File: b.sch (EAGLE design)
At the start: 64 parts, among them CN1 CON-2P-DG500-5.08, CN2 CON-3P-DG500-5.08, CN3 CON-2P-DG500-5.08, CN4 CON-3P-DG500-5.08, CN5 CON-2P-DG500-5.08, Q1 BCR133, U2 TPS563200, U3 ISO3082, U4 B1212S-1WR3, U5 L78L05ACD13TR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

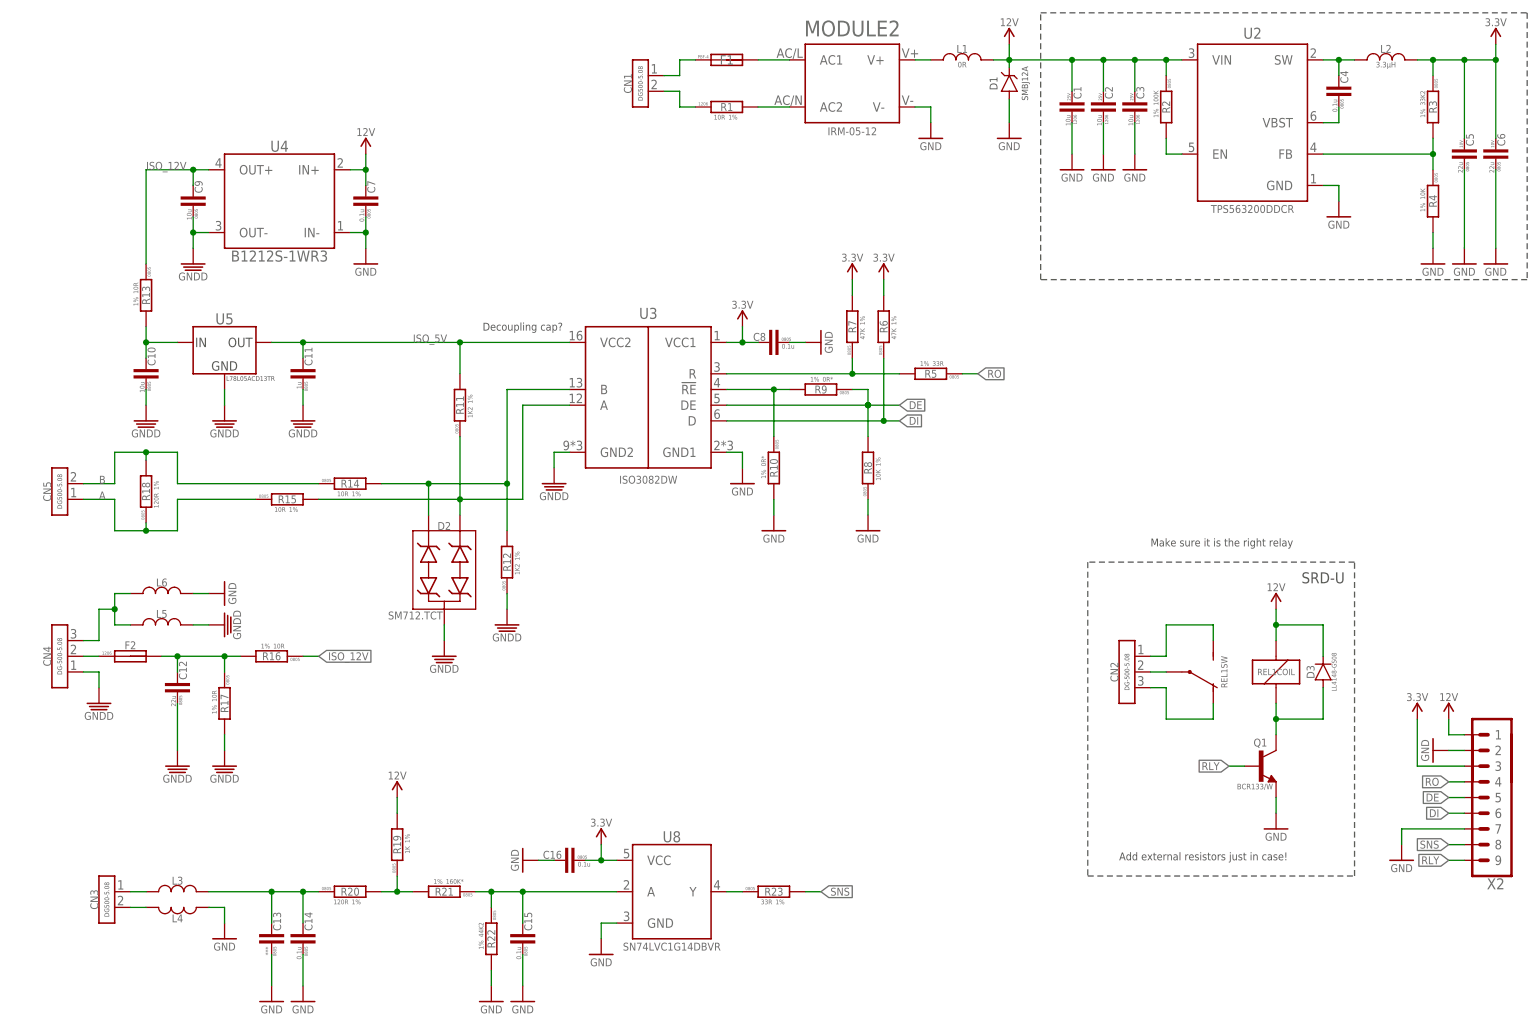
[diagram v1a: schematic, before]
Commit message: Notes and pictures update
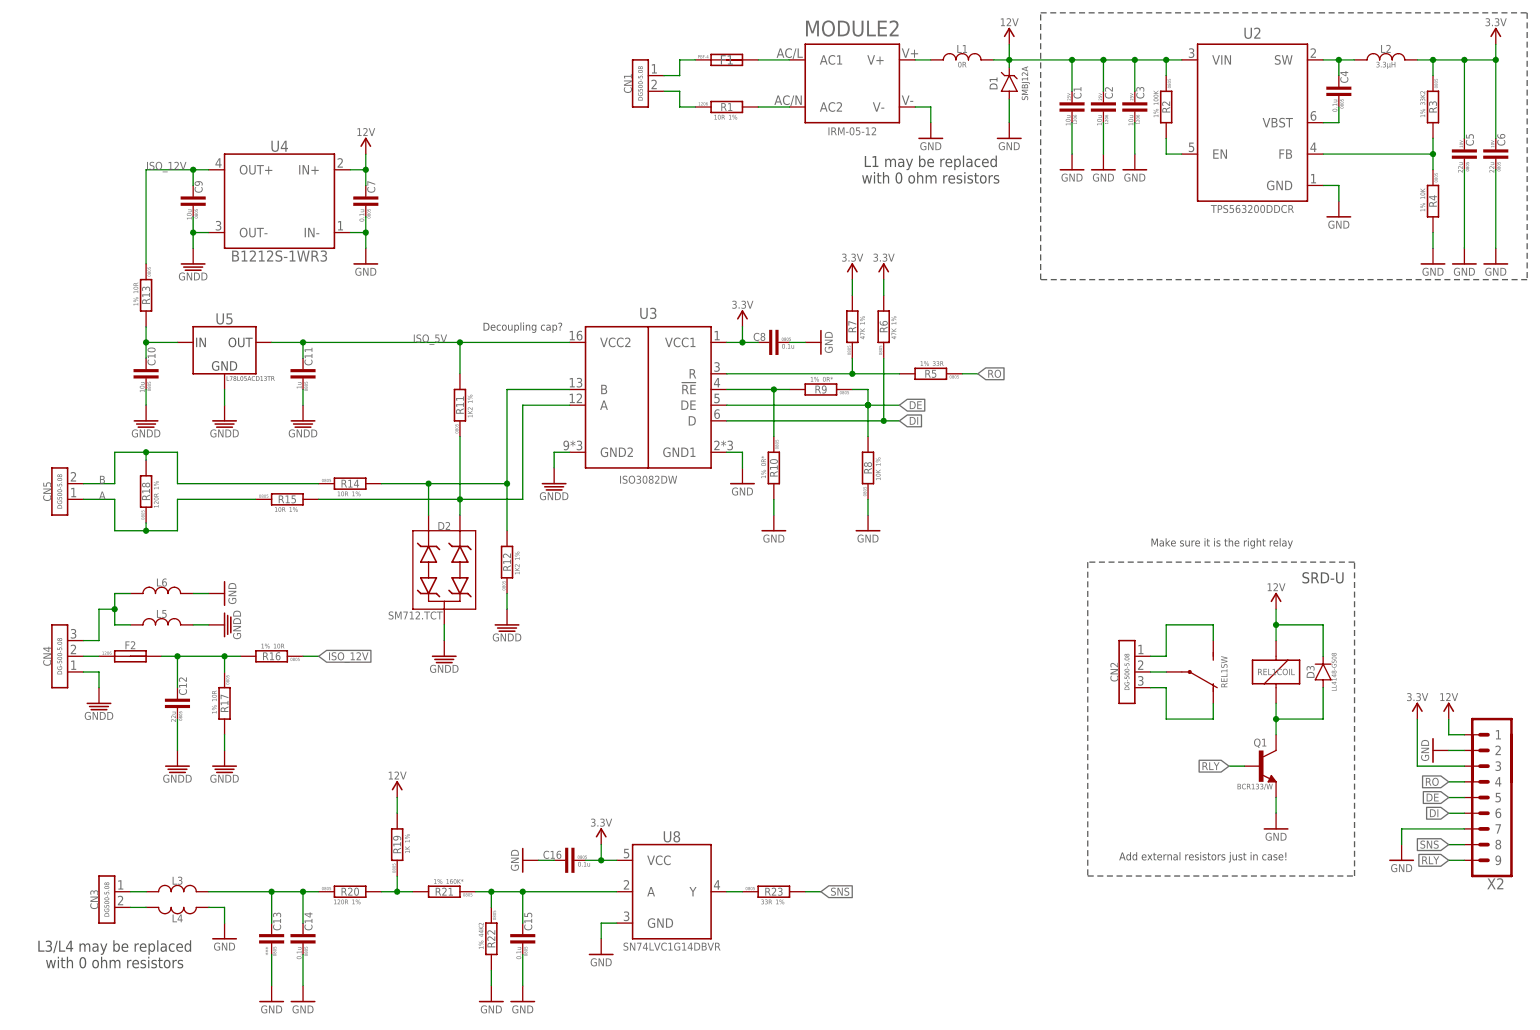
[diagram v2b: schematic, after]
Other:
- note added: "L1 may be replaced with 0 ohm resistors"
- note added: "L3/L4 may be replaced with 0 ohm resistors"
- moved on the sheet: C12
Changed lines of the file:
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@@
 </attributes>
 <variantdefs>
+<variantdef name="basic" current="yes"/>
 </variantdefs>
 <classes>
@@
 <part name="L3" library="rc" library_urn="urn:adsk.eagle:library:2539423" deviceset="L" device="-0805" package3d_urn="urn:adsk.eagle:package:32710307/2"/>
 <part name="L4" library="rc" library_urn="urn:adsk.eagle:library:2539423" deviceset="L" device="-0805" package3d_urn="urn:adsk.eagle:package:32710307/2"/>
-<part name="C13" library="rc" library_urn="urn:adsk.eagle:library:2539423" deviceset="C" device="-0805" package3d_urn="urn:adsk.eagle:package:2539460/3" value="***"/>
+<part name="C13" library="rc" library_urn="urn:adsk.eagle:library:2539423" deviceset="C" device="-0805" package3d_urn="urn:adsk.eagle:package:2539460/3" value="***">
+<variant name="basic" populate="no"/>
+</part>
 <part name="C14" library="rc" library_urn="urn:adsk.eagle:library:2539423" deviceset="C" device="-0805" package3d_urn="urn:adsk.eagle:package:2539460/3" value="0.1u"/>
 <part name="R20" library="rc" library_urn="urn:adsk.eagle:library:2539423" deviceset="R" device="-0805" package3d_urn="urn:adsk.eagle:package:2539455/2" technology="-1%" value="120R"/>
@@
 <part name="GND32" library="supply_symbols" library_urn="urn:adsk.eagle:library:5017758" deviceset="GND" device="" value="GND"/>
 <part name="GND33" library="supply_symbols" library_urn="urn:adsk.eagle:library:5017758" deviceset="GND" device="" value="GND"/>
-<part name="L6" library="rc" library_urn="urn:adsk.eagle:library:2539423" deviceset="L" device="-0805" package3d_urn="urn:adsk.eagle:package:32710307/2"/>
+<part name="L6" library="rc" library_urn="urn:adsk.eagle:library:2539423" deviceset="L" device="-0805" package3d_urn="urn:adsk.eagle:package:32710307/2">
+<variant name="basic" populate="no"/>
+</part>
 <part name="GND35" library="supply_symbols" library_urn="urn:adsk.eagle:library:5017758" deviceset="GND" device="" value="GND"/>
 <part name="R13" library="rc" library_urn="urn:adsk.eagle:library:2539423" deviceset="R" device="-0805" package3d_urn="urn:adsk.eagle:package:2539455/2" technology="-1%" value="10R"/>
@@
 <text x="88.9" y="119.38" size="1.27" layer="97" font="vector" align="center">Decoupling cap?</text>
 <text x="218.44" y="78.74" size="1.778" layer="97" font="vector" align="center">SRD-U</text>
+<text x="22.86" y="17.78" size="1.778" layer="97" font="vector" align="center">L3/L4 may be replaced
+with 0 ohm resistors</text>
+<text x="154.94" y="144.78" size="1.778" layer="97" font="vector" align="center">L1 may be replaced
+with 0 ohm resistors</text>
 </plain>
 <instances>
@@
 <attribute name="ALLOCATED" x="48.26" y="64.516" size="0.762" layer="97" font="vector" rot="R180" align="center"/>
 </instance>
-<instance part="C12" gate="G$1" x="33.02" y="60.96" smashed="yes" rot="R90">
-<attribute name="NAME" x="33.909" y="62.23" size="1.27" layer="95" font="vector" rot="R90" align="center-left"/>
-<attribute name="VALUE" x="32.766" y="59.69" size="0.762" layer="96" font="vector" rot="R90" align="bottom-right"/>
-<attribute name="PACKAGE" x="33.528" y="58.928" size="0.508" layer="97" font="vector" rot="R270" align="center"/>
-<attribute name="VOLTAGE" x="32.512" y="61.976" size="0.508" layer="97" font="vector" rot="R90" align="center-left"/>
-<attribute name="ALLOCATED" x="30.48" y="60.96" size="0.508" layer="97" font="vector" rot="R90" align="center"/>
+<instance part="C12" gate="G$1" x="33.02" y="58.42" smashed="yes" rot="R90">
+<attribute name="NAME" x="33.909" y="59.69" size="1.27" layer="95" font="vector" rot="R90" align="center-left"/>
+<attribute name="VALUE" x="32.766" y="57.15" size="0.762" layer="96" font="vector" rot="R90" align="bottom-right"/>
+<attribute name="PACKAGE" x="33.528" y="56.388" size="0.508" layer="97" font="vector" rot="R270" align="center"/>
+<attribute name="VOLTAGE" x="32.512" y="59.436" size="0.508" layer="97" font="vector" rot="R90" align="center-left"/>
+<attribute name="ALLOCATED" x="30.48" y="58.42" size="0.508" layer="97" font="vector" rot="R90" align="center"/>
 </instance>
 <instance part="GND36" gate="G$1" x="33.02" y="48.26" smashed="yes">
@@
 <pinref part="GND36" gate="G$1" pin="GNDD"/>
 <pinref part="C12" gate="G$1" pin="1"/>
-<wire x1="33.02" y1="50.8" x2="33.02" y2="58.42" width="0.1524" layer="91"/>
+<wire x1="33.02" y1="50.8" x2="33.02" y2="55.88" width="0.1524" layer="91"/>
 </segment>
 <segment>
@@
 <wire x1="40.64" y1="66.04" x2="33.02" y2="66.04" width="0.1524" layer="91"/>
 <wire x1="33.02" y1="66.04" x2="30.48" y2="66.04" width="0.1524" layer="91"/>
-<wire x1="33.02" y1="63.5" x2="33.02" y2="66.04" width="0.1524" layer="91"/>
+<wire x1="33.02" y1="60.96" x2="33.02" y2="66.04" width="0.1524" layer="91"/>
 <junction x="33.02" y="66.04"/>
 <pinref part="R17" gate="G$1" pin="1"/>
@@
 </drawing>
 <compatibility>
+<note version="6.3" minversion="6.2.2" severity="warning">
+Since Version 6.2.2 text objects can contain more than one line,
+which will not be processed correctly with this version.
+</note>
 <note version="8.2" severity="warning">
 Since Version 8.2, EAGLE supports online libraries. The ids
